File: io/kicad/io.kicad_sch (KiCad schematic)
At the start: 30 parts, among them J1 Conn_01x04_Pin, J5 pcie_98, U1 XC6206P332MR, U2 ESD5344D-TP, U3 B0505MT-1WR4, U4 ADuM1201AR, U5 ESD5344D-TP, U6 XC6206P332MR

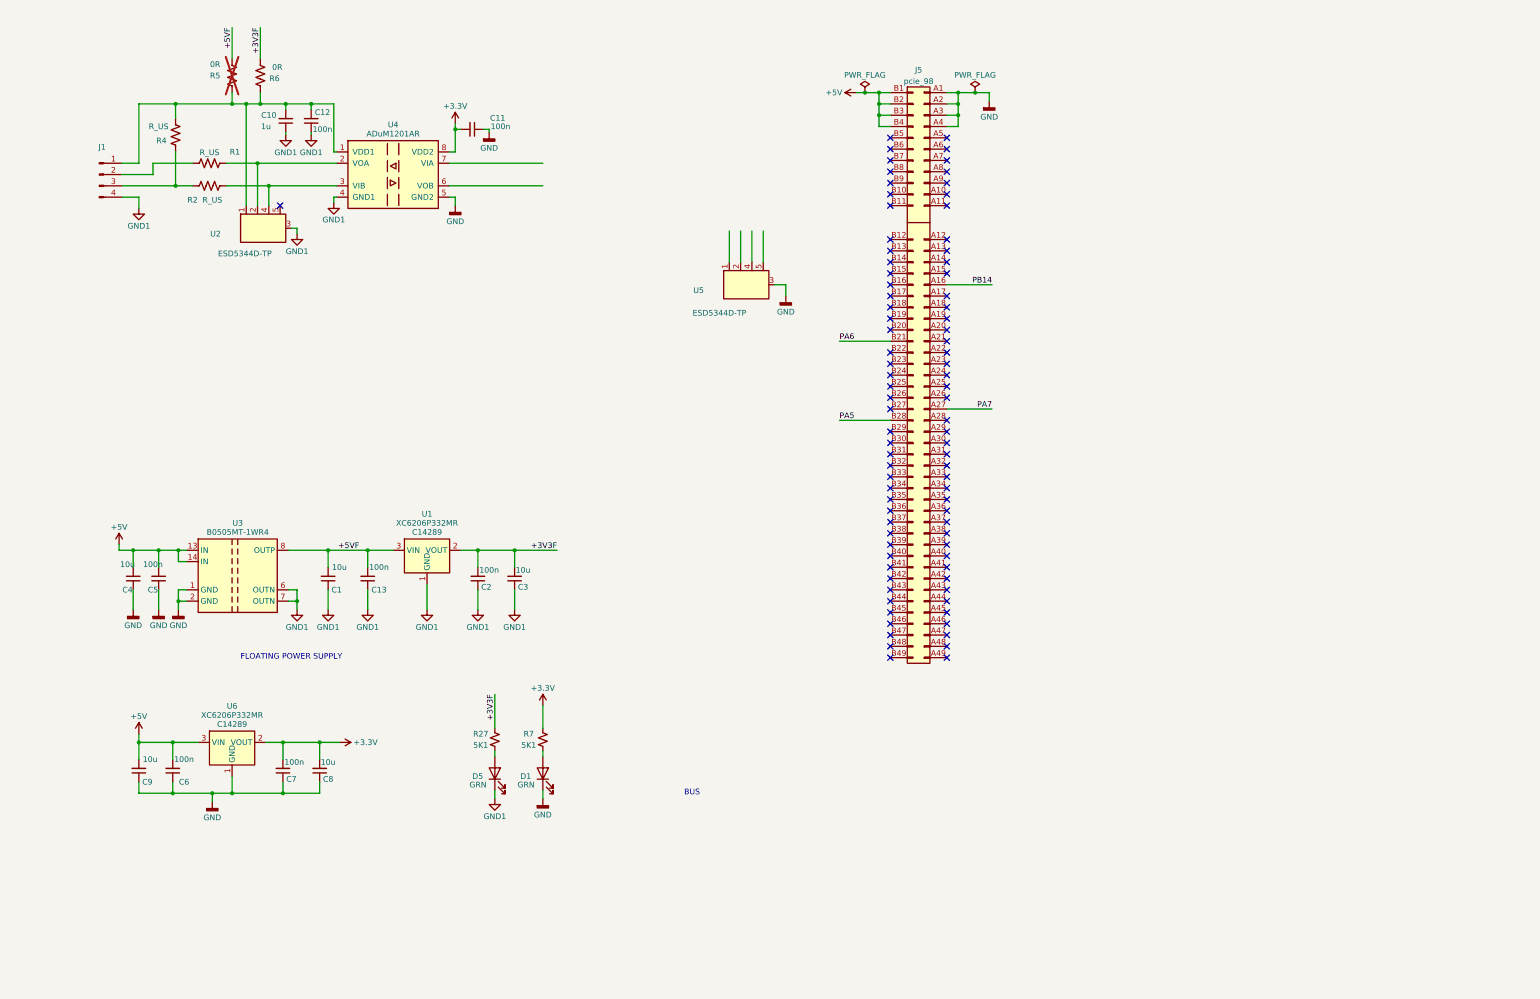
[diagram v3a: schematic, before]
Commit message: IO board schematic is feature complete.
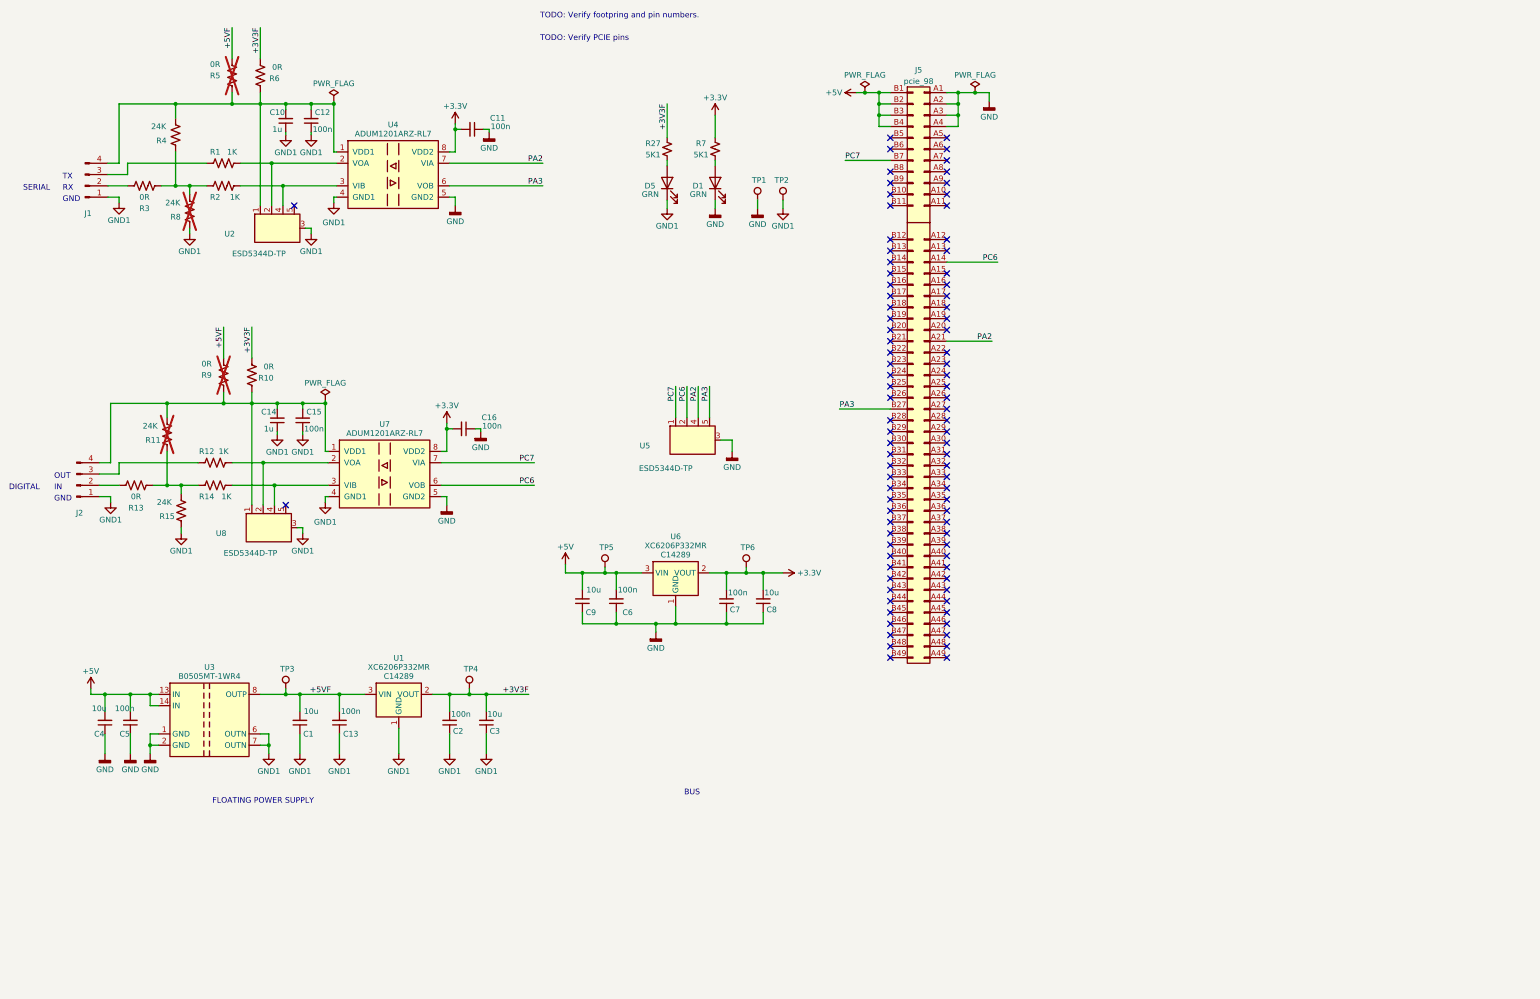
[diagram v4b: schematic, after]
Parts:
- added C14: 1u, Capacitor_SMD:C_0603_1608Metric_Pad1.08x0.95mm_HandSolder, symbol Device:C_Small
- added C15, C16: 100n, Capacitor_SMD:C_0603_1608Metric_Pad1.08x0.95mm_HandSolder, symbol Device:C_Small
- added J2: Conn_01x04_Pin, common:connector_4pins_horizontal, symbol Connector:Conn_01x04_Pin
- added R10, R13, R3, R9: 0R, Resistor_SMD:R_0603_1608Metric_Pad0.98x0.95mm_HandSolder, symbol Device:R_US
- added R11, R15, R8: 24K, Resistor_SMD:R_0603_1608Metric_Pad0.98x0.95mm_HandSolder, symbol Device:R_US
- added R12, R14: 1K, Resistor_SMD:R_0603_1608Metric_Pad0.98x0.95mm_HandSolder, symbol Device:R_US
- added TP1, TP2, TP3, TP4, TP5, TP6: TestPoint, common:Test_Pad, symbol common:TestPoint
- added U7: ADUM1201ARZ-RL7, Package_SO:SOIC-8_3.9x4.9mm_P1.27mm, symbol Isolator:ADuM1201AR
- added U8: ESD5344D-TP, common:Diodes_UDFN-10_1.0x2.5mm_P0.5mm, symbol common:ESD5344D
- C1, C3, C4, C8, C9: footprint Capacitor_SMD:C_0402_1005Metric -> Capacitor_SMD:C_0603_1608Metric_Pad1.08x0.95mm_HandSolder; LCSC (none) -> C96446
- C10: footprint Capacitor_SMD:C_0402_1005Metric -> Capacitor_SMD:C_0603_1608Metric_Pad1.08x0.95mm_HandSolder; LCSC (none) -> C15849
- C11, C12, C13, C2, C5, C6, C7: footprint Capacitor_SMD:C_0402_1005Metric -> Capacitor_SMD:C_0603_1608Metric_Pad1.08x0.95mm_HandSolder; LCSC (none) -> C14663
- J1: footprint (none) -> common:connector_4pins_horizontal; LCSC (none) -> C31753
- R1, R2: value R_US -> 1K; footprint (none) -> Resistor_SMD:R_0603_1608Metric_Pad0.98x0.95mm_HandSolder; LCSC (none) -> C21190
- R27, R7: footprint Resistor_SMD:R_0402_1005Metric -> Resistor_SMD:R_0603_1608Metric_Pad0.98x0.95mm_HandSolder; LCSC C25905 -> C23186
- R4: value R_US -> 24K; footprint (none) -> Resistor_SMD:R_0603_1608Metric_Pad0.98x0.95mm_HandSolder; LCSC (none) -> C23352
- R5, R6: footprint (none) -> Resistor_SMD:R_0603_1608Metric_Pad0.98x0.95mm_HandSolder; LCSC (none) -> C21189
- U3: footprint (none) -> io:Converter_DCDC; LCSC (none) -> C919693
- U4: value ADuM1201AR -> ADUM1201ARZ-RL7; LCSC (none) -> C9669
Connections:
- net +3.3V: now also C16.2, TP6.1, U7.8 (VDD2)
- net +3V3F: now also R10.2, TP4.1
- net +5V: now also TP5.1
- net +5VF: now also R9.2, TP3.1
- net GND: now also C16.1, TP1.1, U7.5 (GND2)
- net GND1: now also J1.1 (Pin_1), C14.1, C15.1, J2.1 (Pin_1), R15.1, R8.1, TP2.1, U7.4 (GND1), U8.3 (GND); no longer J1.4 (Pin_4)
- net at R2.1, R4.1: now also R3.1, R8.2; no longer J1.3 (Pin_3)
- net at C10.2, C12.2, R4.2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: now also J1.4 (Pin_4); no longer J1.1 (Pin_1)
- net PC6: now reaches J5.A14 (Pin_a14)
- net PC6: now also U5.2 (D2), U7.6 (VOB)
- net PA2: now reaches J5.A21 (Pin_a21)
- net PA2: now also U4.7 (VIA), U5.4 (D3)
- net PA3: now reaches J5.B27 (Pin_b27)
- net PA3: now also U4.6 (VOB), U5.5 (D4)
- net PC7: now reaches J5.B7 (Pin_b7)
- net PC7: now also U5.1 (D1), U7.7 (VIA)
- net at J1.2 (Pin_2): now also R3.2; no longer R1.1
- net PA5: no longer names the net of J5.B28 (Pin_b28)
- net PA6: no longer names the net of J5.B21 (Pin_b21)
- net PA7: no longer names the net of J5.A27 (Pin_a27)
- net PB14: no longer names the net of J5.A16 (Pin_a16)
- new net: R11.1, R13.1, R14.1, R15.2
- new net: J2.2 (Pin_2), R13.2
- new net: C14.2, C15.2, J2.4 (Pin_4), R10.1, R11.2, R9.1, U7.1 (VDD1), U8.1 (D1)
- new net: R12.2, U7.2 (VOA), U8.2 (D2)
- new net: R14.2, U7.3 (VIB), U8.4 (D3)
- new net: J1.3 (Pin_3), R1.1
- new net: J2.3 (Pin_3), R12.1
- no-connect marks 87 -> 88
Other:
- note added: "DIGITAL"
- note added: "GND"
- note added: "IN"
- note added: "OUT"
- note added: "RX"
- note added: "SERIAL"
- note added: "TODO: Verify PCIE pins"
- note added: "TODO: Verify footpring and pin numbers."
- note added: "TX"
- moved on the sheet: C1, C13, C2, C3, C4, C5, C6, C7, C8, C9, D1, D5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

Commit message: Work in progress. Placement of the IO board.
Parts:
- renumbered C4 to C1, C16 to C10, C3 to C12, C9 to C13, C6 to C14, C7 to C15, C8 to C16, C5 to C2, C14 to C3, C10 to C4, C1 to C5, C15 to C6, C12 to C7, C13 to C8, C2 to C9, D5 to D1, D1 to D2, J2 to J1, J1 to J2, J5 to J3, R13 to R1, R2 to R10, R9 to R11, R5 to R12, R10 to R13, R6 to R14, R27 to R15, R7 to R16, R3 to R2, R11 to R3, R15 to R5, R8 to R6, R12 to R7, R14 to R8, R1 to R9, TP3 to TP1, TP4 to TP2, TP5 to TP3, TP6 to TP4, TP1 to TP5, TP2 to TP6, U3 to U1, U8 to U2, U2 to U3, U7 to U4, U4 to U5, U1 to U6, U6 to U7, U5 to U8
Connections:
- net GND1: now also J1.4 (Pin_4), J2.4 (Pin_4); no longer J1.1 (Pin_1), J2.1 (Pin_1)
- net at C4.2, C7.2, R12.1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: now also J2.1 (Pin_1); no longer J2.4 (Pin_4)
- net at R1.2: now also J1.3 (Pin_3); no longer J1.2 (Pin_2)
- net at C3.2, C6.2, R11.1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: now also J1.1 (Pin_1); no longer J1.4 (Pin_4)
- net at R2.2: now also J2.3 (Pin_3); no longer J2.2 (Pin_2)
- net at R9.1: now also J2.2 (Pin_2); no longer J2.3 (Pin_3)
- net at R7.1: now also J1.2 (Pin_2); no longer J1.3 (Pin_3)

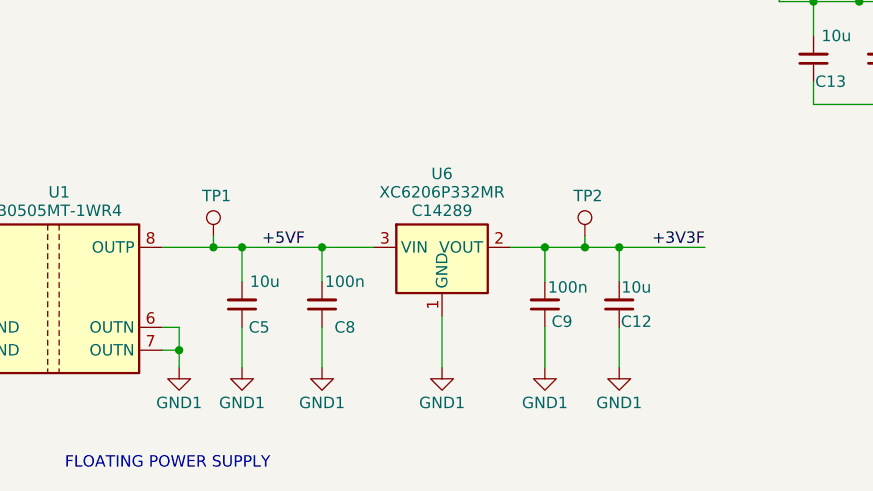
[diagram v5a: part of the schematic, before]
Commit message: IO layout passes DRC.
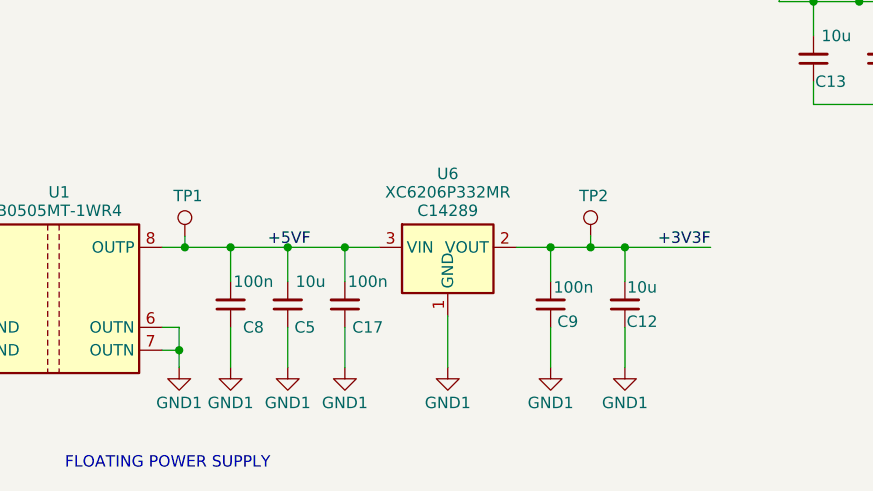
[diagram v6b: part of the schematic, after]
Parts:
- added C17: 100n, Capacitor_SMD:C_0603_1608Metric_Pad1.08x0.95mm_HandSolder, symbol Device:C_Small
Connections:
- net +5VF: now also C17.2
- net GND1: now also C17.1
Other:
- moved on the sheet: C12, C5, C8, C9, TP1, TP2, U6

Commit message: Tweaked IO board layout.
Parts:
- U4, U5: JLCRotOffset (none) -> -90
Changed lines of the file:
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@@
+      (effects (font (size 1.27 1.27)) hide)
+    )
+    (property "JLCRotOffset" "-90" (at 101.6 120.015 0)
       (effects (font (size 1.27 1.27)) hide)
     )
@@
       (effects (font (size 1.27 1.27)) hide)
     )
+    (property "JLCRotOffset" "-90" (at 103.505 52.705 0)
+      (effects (font (size 1.27 1.27)) hide)
+    )

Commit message: Updated JLCPCB part positioning.
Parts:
- U6, U7: JLCRotOffset (none) -> 180
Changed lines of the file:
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@@
       (effects (font (size 1.27 1.27)))
+    )
+    (property "JLCRotOffset" "180" (at 105.41 172.085 0)
+      (effects (font (size 1.27 1.27)) hide)
     )
     (pin "1")
@@
       (effects (font (size 1.27 1.27)))
     )
-    (pin "1")
+    (property "JLCRotOffset" "180" (at 167.005 144.78 0)
+      (effects (font (size 1.27 1.27)) hide)
+    )
+    (pin "1")
